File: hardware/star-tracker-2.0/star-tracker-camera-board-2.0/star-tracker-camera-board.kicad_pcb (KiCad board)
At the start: 4 copper layers, 31.5 x 13.6 mm, 43 parts, among them J1 3-1734742-6, U1 AR0134CSSM00SPCA0, U2 TPS70618DRVR, U3 TPS71928-28DRVT, U4 TPS71928-28DRVT, X1 MC2520Z27.0000C19XSH

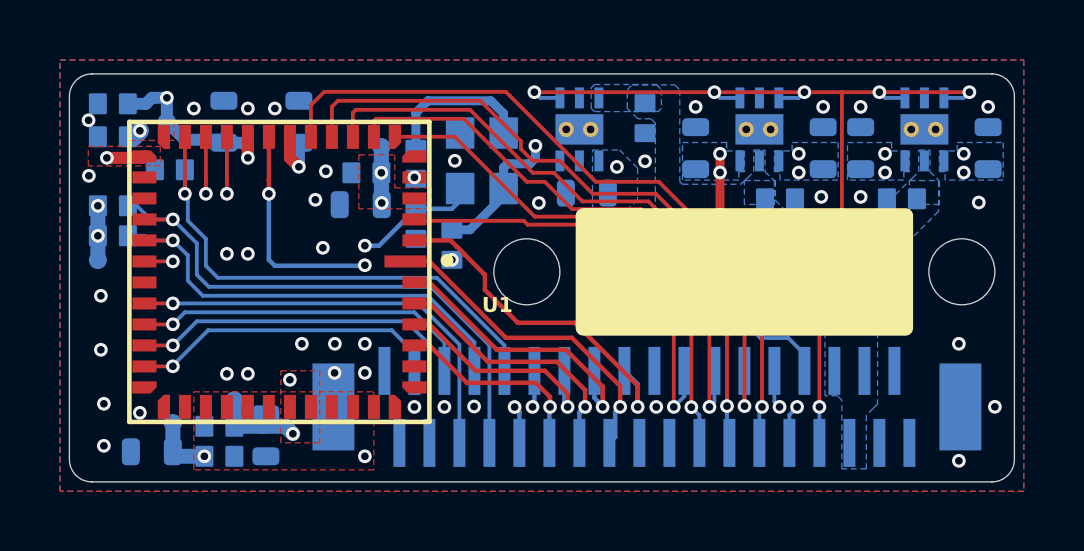
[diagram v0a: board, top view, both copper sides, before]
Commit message: Bom update
Updated BOM to correct connector MPN and other misc components
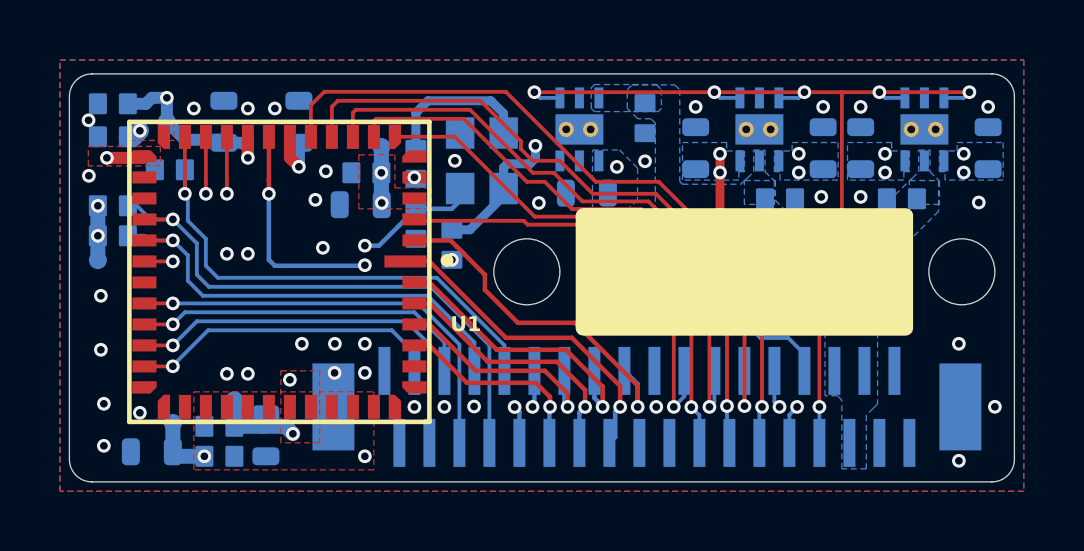
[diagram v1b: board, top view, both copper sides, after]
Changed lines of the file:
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@@
 		(at 139.7511 104.8036 -90)
 		(property "Reference" "U1"
-			(at 1.3964 -6.7489 0)
+			(at 2.0364 -5.6989 0)
 			(layer "F.SilkS")
 			(effects
@@
 		(descr "<b>e0402 (metric 1005) normal 'IPC-B' without silkscreen</b>\n<br>In house package for nominal spacing based on IPC-7351B.\nThis package is identical to 0402-B, but has its tPlace silkscreen layer removed.")
 		(property "Reference" "C9"
-			(at -0.8 0.55 0)
+			(at 0.24 0.55 0)
 			(layer "B.SilkS")
 			(effects
@@
 		(descr "<b>e0402 (metric 1005) normal 'IPC-B' without silkscreen</b>\n<br>In house package for nominal spacing based on IPC-7351B.\nThis package is identical to 0402-B, but has its tPlace silkscreen layer removed.")
 		(property "Reference" "C7"
-			(at -0.8 0.55 0)
+			(at -3.02 -0.22 0)
 			(layer "B.SilkS")
 			(effects
@@
 		(descr "TEST PAD")
 		(property "Reference" "TP4"
-			(at 0.75 1.79 90)
+			(at 0.01 2.04 90)
 			(unlocked yes)
 			(layer "B.SilkS")
@@
 		(descr "TEST PAD")
 		(property "Reference" "TP2"
-			(at -1.24 -0.75 0)
+			(at -0.59 -0.75 0)
 			(unlocked yes)
 			(layer "B.SilkS")
@@
 		(descr "<b>0603 (metric 1608) tight 'IPC-C' without silkscreen</b>\n<br>In house package for minimum spacing based on IPC-7351B.\nThis package is identical to 0603-C, but has its tPlace silkscreen layer removed.")
 		(property "Reference" "C5"
-			(at 0.6 0.5 0)
+			(at -0.18 0.68 0)
 			(layer "B.SilkS")
 			(effects
@@
 		(descr "<b>e0402 (metric 1005) normal 'IPC-B' without silkscreen</b>\n<br>In house package for nominal spacing based on IPC-7351B.\nThis package is identical to 0402-B, but has its tPlace silkscreen layer removed.")
 		(property "Reference" "R6"
-			(at -0.8 0.55 270)
+			(at 2.13 0.34 270)
 			(layer "B.SilkS")
 			(effects
@@
 		(descr "<b>e0402 (metric 1005) normal 'IPC-B' without silkscreen</b>\n<br>In house package for nominal spacing based on IPC-7351B.\nThis package is identical to 0402-B, but has its tPlace silkscreen layer removed.")
 		(property "Reference" "R4"
-			(at -0.8 0.55 270)
+			(at -0.8 0.32 270)
 			(layer "B.SilkS")
 			(effects
@@
 		(descr "<b>0603 (metric 1608) tight 'IPC-C' without silkscreen</b>\n<br>In house package for minimum spacing based on IPC-7351B.\nThis package is identical to 0603-C, but has its tPlace silkscreen layer removed.")
 		(property "Reference" "C6"
-			(at -2.9 -0.25 90)
+			(at -2.35 -0.32 90)
 			(layer "B.SilkS")
 			(effects
@@
 		(descr "TEST PAD")
 		(property "Reference" "TP5"
-			(at 0.3 0.38 90)
+			(at 0.26 0.38 90)
 			(unlocked yes)
 			(layer "B.SilkS")
@@
 		(descr "TEST PAD")
 		(property "Reference" "TP1"
-			(at -1 -1.05 0)
+			(at -0.73 -1.07 0)
 			(unlocked yes)
 			(layer "B.SilkS")
@@
 		(descr "<b>0603 (metric 1608) tight 'IPC-C' without silkscreen</b>\n<br>In house package for minimum spacing based on IPC-7351B.\nThis package is identical to 0603-C, but has its tPlace silkscreen layer removed.")
 		(property "Reference" "C19"
-			(at -0.6489 -1.2214 0)
+			(at -0.6489 -1.3214 0)
 			(layer "B.SilkS")
 			(effects
@@
 		(descr "<b>e0402 (metric 1005) normal 'IPC-B' without silkscreen</b>\n<br>In house package for nominal spacing based on IPC-7351B.\nThis package is identical to 0402-B, but has its tPlace silkscreen layer removed.")
 		(property "Reference" "C18"
-			(at -0.8 0.55 90)
+			(at -0.9886 -1.0914 90)
 			(layer "B.SilkS")
 			(effects
@@
 		(descr "<b>e0402 (metric 1005) normal 'IPC-B' without silkscreen</b>\n<br>In house package for nominal spacing based on IPC-7351B.\nThis package is identical to 0402-B, but has its tPlace silkscreen layer removed.")
 		(property "Reference" "C16"
-			(at -0.8 0.55 0)
+			(at -2.3689 -0.2539 0)
 			(layer "B.SilkS")
 			(effects
@@
 		(descr "<b>e0402 (metric 1005) normal 'IPC-B' without silkscreen</b>\n<br>In house package for nominal spacing based on IPC-7351B.\nThis package is identical to 0402-B, but has its tPlace silkscreen layer removed.")
 		(property "Reference" "R2"
-			(at -0.8 0.55 180)
+			(at 2.04 0.28 180)
 			(layer "B.SilkS")
 			(effects
@@
 		(descr "<b>e0402 (metric 1005) normal 'IPC-B' without silkscreen</b>\n<br>In house package for nominal spacing based on IPC-7351B.\nThis package is identical to 0402-B, but has its tPlace silkscreen layer removed.")
 		(property "Reference" "C14"
-			(at -0.8 0.55 180)
+			(at -1.0186 0.3339 180)
 			(layer "B.SilkS")
 			(effects
@@
 		(descr "<b>e0402 (metric 1005) normal 'IPC-B' without silkscreen</b>\n<br>In house package for nominal spacing based on IPC-7351B.\nThis package is identical to 0402-B, but has its tPlace silkscreen layer removed.")
 		(property "Reference" "R5"
-			(at -0.8 0.55 270)
+			(at 2.13 0.34 270)
 			(layer "B.SilkS")
 			(effects
@@
 		(descr "<b>e0402 (metric 1005) normal 'IPC-B' without silkscreen</b>\n<br>In house package for nominal spacing based on IPC-7351B.\nThis package is identical to 0402-B, but has its tPlace silkscreen layer removed.")
 		(property "Reference" "R10"
-			(at -0.8 0.55 270)
+			(at 2.4536 0.28 270)
 			(layer "B.SilkS")
 			(effects
@@
 		(descr "<b>e0402 (metric 1005) normal 'IPC-B' without silkscreen</b>\n<br>In house package for nominal spacing based on IPC-7351B.\nThis package is identical to 0402-B, but has its tPlace silkscreen layer removed.")
 		(property "Reference" "C13"
-			(at -0.8 0.55 0)
+			(at -0.1 1.46 0)
 			(layer "B.SilkS")
 			(effects
@@
 		(descr "<b>e0402 (metric 1005) normal 'IPC-B' without silkscreen</b>\n<br>In house package for nominal spacing based on IPC-7351B.\nThis package is identical to 0402-B, but has its tPlace silkscreen layer removed.")
 		(property "Reference" "R3"
-			(at -0.8 0.55 0)
+			(at -1.98 -0.32 0)
 			(layer "B.SilkS")
 			(effects
@@
 		(descr "<b>e0402 (metric 1005) normal 'IPC-B' without silkscreen</b>\n<br>In house package for nominal spacing based on IPC-7351B.\nThis package is identical to 0402-B, but has its tPlace silkscreen layer removed.")
 		(property "Reference" "C11"
-			(at -0.8 0.55 180)
+			(at 0.06 -1.66 180)
 			(layer "B.SilkS")
 			(effects
@@
 		(descr "<b>e0402 (metric 1005) normal 'IPC-B' without silkscreen</b>\n<br>In house package for nominal spacing based on IPC-7351B.\nThis package is identical to 0402-B, but has its tPlace silkscreen layer removed.")
 		(property "Reference" "R7"
-			(at -0.8 0.55 90)
+			(at -1.99 -0.32 90)
 			(layer "B.SilkS")
 			(effects
@@
 		(descr "e0402 (metric 1005) normal 'IPC-B' without silkscreen\nIn house package for nominal spacing based on IPC-7351B. This package is identical to 0402-B, but has its tPlace silkscreen layer removed.")
 		(property "Reference" "R11"
-			(at -1.5036 0 90)
+			(at -1.6236 0 90)
 			(unlocked yes)
 			(layer "B.SilkS")
@@
 		(descr "<b>e0402 (metric 1005) normal 'IPC-B' without silkscreen</b>\n<br>In house package for nominal spacing based on IPC-7351B.\nThis package is identical to 0402-B, but has its tPlace silkscreen layer removed.")
 		(property "Reference" "R9"
-			(at -0.8 0.55 90)
+			(at -2.0836 -0.38 90)
 			(layer "B.SilkS")
 			(effects
@@
 		(descr "<b>e0402 (metric 1005) normal 'IPC-B' without silkscreen</b>\n<br>In house package for nominal spacing based on IPC-7351B.\nThis package is identical to 0402-B, but has its tPlace silkscreen layer removed.")
 		(property "Reference" "C1"
-			(at -0.8 0.55 270)
+			(at -0.8 0.3 270)
 			(layer "B.SilkS")
 			(effects
@@
 		(descr "<b>e0402 (metric 1005) normal 'IPC-B' without silkscreen</b>\n<br>In house package for nominal spacing based on IPC-7351B.\nThis package is identical to 0402-B, but has its tPlace silkscreen layer removed.")
 		(property "Reference" "C8"
-			(at -0.8 0.55 0)
+			(at -0.9 -1.06 0)
 			(layer "B.SilkS")
 			(effects

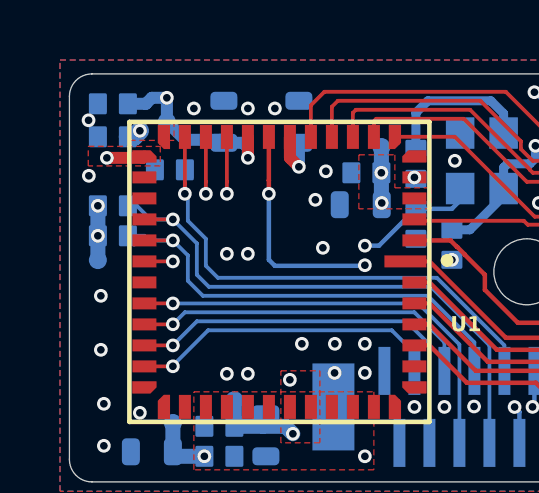
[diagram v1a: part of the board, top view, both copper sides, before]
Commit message: Update to Camera Board
Update BOM for camera board, replaced lower tier dielectric caps to X7R
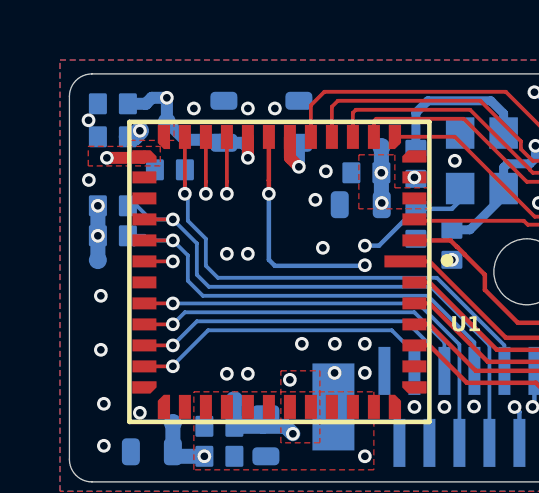
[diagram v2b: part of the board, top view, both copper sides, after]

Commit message: Finishing touches
added gitignore for .ds_store (mac file for kicad) changed bom details for components. added 3d models to footprints. Went over schematic checklist. Camera and star tracker ready for final DR for send off.
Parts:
- U1: value AR0134CSSM00SPCA0 -> Val**
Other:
- board text added: "OCB v${REVISION} ${ISSUE_DATE}"
- board text removed: "OCB v${REVISION} OR et al ${ISSUE_DATE}"
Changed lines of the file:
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@@
 	(title_block
 		(title "OreSat Star Tracker Camera Board")
-		(date "2026-04-22")
-		(rev "4.1")
+		(date "2026-06-19")
+		(rev "4.2")
 		(company "Portland State Aerospace Society")
 	)
@@
 			)
 		)
-		(property "Value" "AR0134CSSM00SPCA0"
+		(property "Value" "Val**"
 			(at 0 0 90)
 			(layer "F.Fab")
@@
 		(sheetname "/")
 		(sheetfile "star-tracker-camera-board.kicad_sch")
-		(units
-			(unit
-				(name "A")
-				(pins "5" "22" "27" "23" "17" "15" "16" "24" "19" "14" "20" "21" "41"
-					"31" "32" "33" "42" "43" "18" "12" "6" "25" "30" "44" "4" "35" "39"
-					"34" "36" "40" "38" "37" "45" "46" "47" "48" "1" "2" "3" "7" "8" "9"
-					"10" "11" "29" "28" "13" "26"
-				)
-			)
-		)
 		(duplicate_pad_numbers_are_jumpers no)
 		(fp_poly
@@
 		)
 		(embedded_fonts no)
-		(model "C:/Users/Edward/Desktop/AR0134CSSC00SPCA0-DPBR.stp"
+		(model "${ORESAT_LIBRARIES}/oresat-3dmodels/AR0134CSSC00SPCA0-DPBR.stp"
 			(offset
 				(xyz 0 0 0)
@@
 		)
 		(embedded_fonts no)
-		(model "C:/Users/Edward/Desktop/RC0402FR-07226RL.STEP"
+		(model "${ORESAT_LIBRARIES}/oresat-3dmodels/RC0402FR-07226RL.STEP"
 			(offset
 				(xyz 0 0 0)
@@
 		)
 		(embedded_fonts no)
-		(model "C:/Users/Edward/Desktop/RC0402FR-07226RL.STEP"
+		(model "${ORESAT_LIBRARIES}/oresat-3dmodels/RC0402FR-07226RL.STEP"
 			(offset
 				(xyz 0 0 0)
@@
 		)
 		(embedded_fonts no)
-		(model "C:/Users/Edward/Desktop/RC0402FR-07226RL.STEP"
+		(model "${ORESAT_LIBRARIES}/oresat-3dmodels/RC0402FR-07226RL.STEP"
 			(offset
 				(xyz 0 0 0)
@@
 		)
 		(embedded_fonts no)
-		(model "C:/Users/Edward/Desktop/RC0402FR-07226RL.STEP"
+		(model "${ORESAT_LIBRARIES}/oresat-3dmodels/RC0402FR-07226RL.STEP"
 			(offset
 				(xyz 0 0 0)
@@
 		)
 		(embedded_fonts no)
-		(model "C:/Users/Edward/Desktop/RC0402FR-07226RL.STEP"
+		(model "${ORESAT_LIBRARIES}/oresat-3dmodels/RC0402FR-07226RL.STEP"
 			(offset
 				(xyz 0 0 0)
@@
 		)
 		(embedded_fonts no)
-		(model "C:/Users/Edward/Desktop/RC0402FR-07226RL.STEP"
+		(model "${ORESAT_LIBRARIES}/oresat-3dmodels/RC0402FR-07226RL.STEP"
 			(offset
 				(xyz 0 0 0)
@@
 		)
 		(embedded_fonts no)
-		(model "C:/Users/Edward/Desktop/RC0402FR-07226RL.STEP"
+		(model "${ORESAT_LIBRARIES}/oresat-3dmodels/RC0402FR-07226RL.STEP"
 			(offset
 				(xyz 0 0 0)
@@
 		)
 		(embedded_fonts no)
-		(model "C:/Users/Edward/Desktop/RC0402FR-07226RL.STEP"
+		(model "${ORESAT_LIBRARIES}/oresat-3dmodels/RC0402FR-07226RL.STEP"
 			(offset
 				(xyz 0 0 0)
@@
 		)
 		(embedded_fonts no)
-		(model "C:/Users/Edward/Desktop/RC0402FR-07226RL.STEP"
+		(model "${ORESAT_LIBRARIES}/oresat-3dmodels/RC0402FR-07226RL.STEP"
 			(offset
 				(xyz 0 0 0)
@@
 		)
 		(embedded_fonts no)
-		(model "C:/Users/Edward/Desktop/RC0402FR-07226RL.STEP"
+		(model "${ORESAT_LIBRARIES}/oresat-3dmodels/RC0402FR-07226RL.STEP"
 			(offset
 				(xyz 0 0 0)
@@
 		)
 		(embedded_fonts no)
-		(model "C:/Users/Edward/Desktop/RC0402FR-07226RL.STEP"
+		(model "${ORESAT_LIBRARIES}/oresat-3dmodels/RC0402FR-07226RL.STEP"
 			(offset
 				(xyz 0 0 0)
@@
 		(sheetname "/")
 		(sheetfile "star-tracker-camera-board.kicad_sch")
-		(units
-			(unit
-				(name "A")
-				(pins "4" "6" "2" "3" "5" "7" "8" "9" "1")
-			)
-		)
 		(duplicate_pad_numbers_are_jumpers no)
 		(fp_poly
@@
 		)
 		(embedded_fonts no)
-		(model "C:/Users/Edward/Desktop/DRV0006A.stp"
+		(model "${ORESAT_LIBRARIES}/oresat-3dmodels/DRV0006A.stp"
 			(offset
 				(xyz 0 0 0)
@@
 			)
 			(rotate
-				(xyz 0 0 0)
+				(xyz -0 -0 -0)
 			)
 		)
@@
 		)
 		(embedded_fonts no)
-		(model "C:/Users/Edward/Desktop/RC0402FR-07226RL.STEP"
+		(model "${ORESAT_LIBRARIES}/oresat-3dmodels/RC0402FR-07226RL.STEP"
 			(offset
 				(xyz 0 0 0)
@@
 		)
 		(embedded_fonts no)
-		(model "C:/Users/Edward/Desktop/RC0402FR-07226RL.STEP"
+		(model "${ORESAT_LIBRARIES}/oresat-3dmodels/RC0402FR-07226RL.STEP"
 			(offset
 				(xyz 0 0 0)
@@
 		)
 		(embedded_fonts no)
-		(model "C:/Users/Edward/Desktop/RC0402FR-07226RL.STEP"
+		(model "${ORESAT_LIBRARIES}/oresat-3dmodels/RC0402FR-07226RL.STEP"
 			(offset
 				(xyz 0 0 0)
@@
 		)
 		(embedded_fonts no)
-		(model "C:/Users/Edward/Desktop/RC0402FR-07226RL.STEP"
+		(model "${ORESAT_LIBRARIES}/oresat-3dmodels/RC0402FR-07226RL.STEP"
 			(offset
 				(xyz 0 0 0)
@@
 		)
 		(embedded_fonts no)
-		(model "C:/Users/Edward/Desktop/RC0402FR-07226RL.STEP"
+		(model "${ORESAT_LIBRARIES}/oresat-3dmodels/RC0402FR-07226RL.STEP"
 			(offset
 				(xyz 0 0 0)
@@
 		(sheetname "/")
 		(sheetfile "star-tracker-camera-board.kicad_sch")
-		(units
-			(unit
-				(name "A")
-				(pins "1" "2" "3" "4" "5" "6" "7" "8" "9" "10" "11" "12" "13" "14" "15"
-					"16" "17" "18" "19" "20" "21" "22" "23" "24" "25" "26" "27" "28" "29"
-					"30" "31" "32" "33" "34" "35" "36" "S1" "S2"
-				)
-			)
-		)
 		(duplicate_pad_numbers_are_jumpers no)
 		(fp_line
@@
 		)
 		(embedded_fonts no)
-		(model "C:/Users/Edward/Desktop/c-3-2492144-6-1-3d.stp"
+		(model "${ORESAT_LIBRARIES}/oresat-3dmodels/c-3-2492144-6-1-3d.stp"
 			(offset
 				(xyz -1 0 5)
@@
 		(sheetname "/")
 		(sheetfile "star-tracker-camera-board.kicad_sch")
-		(units
-			(unit
-				(name "A")
-				(pins "6" "4" "2" "5" "7" "8" "9" "1" "3")
-			)
-		)
 		(duplicate_pad_numbers_are_jumpers no)
 		(fp_poly
@@
 		)
 		(embedded_fonts no)
-		(model "C:/Users/Edward/Desktop/DRV0006A.stp"
+		(model "${ORESAT_LIBRARIES}/oresat-3dmodels/DRV0006A.stp"
 			(offset
 				(xyz 0 0 0)
@@
 			)
 			(rotate
-				(xyz 0 0 0)
+				(xyz -0 -0 -0)
 			)
 		)
@@
 		(sheetname "/")
 		(sheetfile "star-tracker-camera-board.kicad_sch")
-		(units
-			(unit
-				(name "A")
-				(pins "6" "4" "2" "5" "7" "8" "9" "1" "3")
-			)
-		)
 		(duplicate_pad_numbers_are_jumpers no)
 		(fp_poly
@@
 		)
 		(embedded_fonts no)
-		(model "C:/Users/Edward/Desktop/DRV0006A.stp"
+		(model "${ORESAT_LIBRARIES}/oresat-3dmodels/DRV0006A.stp"
 			(offset
 				(xyz 0 0 0)
@@
 			)
 			(rotate
-				(xyz 0 0 0)
+				(xyz -0 -0 -0)
 			)
 		)
@@
 		)
 		(embedded_fonts no)
-		(model "C:/Users/Edward/Desktop/RC0402FR-07226RL.STEP"
+		(model "${ORESAT_LIBRARIES}/oresat-3dmodels/RC0402FR-07226RL.STEP"
 			(offset
 				(xyz 0 0 0)
@@
 		)
 		(embedded_fonts no)
-		(model "C:/Users/Edward/Desktop/RC0402FR-07226RL.STEP"
+		(model "${ORESAT_LIBRARIES}/oresat-3dmodels/RC0402FR-07226RL.STEP"
 			(offset
 				(xyz 0 0 0)
@@
 		)
 	)
-	(gr_text "OCB v${REVISION}\nOR et al\n${ISSUE_DATE}"
+	(gr_text "OCB v${REVISION}\n${ISSUE_DATE}"
 		(at 137.95 105.8 0)
 		(layer "B.SilkS")
@@
 		(priority 10)
 		(connect_pads yes
-			(clearance 0.000001)
+			(clearance 0.2)
 		)
-		(min_thickness 0.0635)
+		(min_thickness 0.127)
 		(fill yes
-			(thermal_gap 0.5)
+			(thermal_gap 0.127)
 			(thermal_bridge_width 0.5)
+			(smoothing fillet)
+			(radius 0.2)
 			(island_removal_mode 0)
 		)

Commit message: Minor Alterations
small change to PCB and silkscreen placement/component routing.
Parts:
- U1: value Val** -> AR0134CSSM00SPCA0
- turned R1 to 0 degrees
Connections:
- R1 pad 1: /STANDBY -> VDD_IO
- R1 pad 2: VDD_IO -> /STANDBY
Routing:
- net /D7: track 17.5 -> 18.3 mm
- net /D8: track 19.5 -> 20.2 mm
- net /D9: track 21.1 -> 21.7 mm
- net GND: vias 45 -> 44
